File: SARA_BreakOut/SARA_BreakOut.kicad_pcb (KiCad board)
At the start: 2 copper layers, 82 parts, among them J1 USB_B, J12 Batt_conn, J13 3v8 tp, J14 1v8 tp, J15 Mechanical_slot, J16 1,2:Vusb_bat/3,4:Vxplain, J17 priority1_1,2:on/3,4:off, J18 priority2_1,2:on/3,4:off, J2 Conn_02x10_Odd_Even, J3 cur_tp, J4 txd, J5 rxd, J6 pwr_on, J7 reset_n, J8 EXT_BATT, J9 conn_to_board, SW1 SW_Push, SW2 SW_Push, U1 LSF0108, U2 LSF0108, U3 AP7361C-SOT89-5, U4 SARA-R410M-02B, U5 TLV62568A, U6 SWISSCOM_SIM

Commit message: first finish of pcb
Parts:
- removed D10: network, LEDs:LED_1206_HandSoldering
- removed D11: mod_status, LEDs:LED_1206_HandSoldering
- removed D12: sim, LEDs:LED_1206_HandSoldering
- removed D6: sara_tx, LEDs:LED_1206_HandSoldering
- removed D7: sara_rx, LEDs:LED_1206_HandSoldering
- removed D8: pwr_on, LEDs:LED_1206_HandSoldering
- removed D9: v_int, LEDs:LED_1206_HandSoldering
- removed J17: priority1_1,2:on/3,4:off, Pin_Headers:Pin_Header_Angled_2x02_Pitch2.54mm
- removed J18: priority2_1,2:on/3,4:off, Pin_Headers:Pin_Header_Angled_2x02_Pitch2.54mm
- removed R10, R11, R12, R13, R14, R15, R9: 2k, Resistors_SMD:R_1206_HandSoldering
- BT1, C24, C3, C4, C5, L1, R4, R5, R6, R7, R8, U3, U5: moved to B.Cu
- J12: footprint Pin_Headers:Pin_Header_Angled_1x02_Pitch2.54mm -> Pin_Headers:Pin_Header_Straight_1x02_Pitch2.54mm
- J16: footprint Pin_Headers:Pin_Header_Angled_2x02_Pitch2.54mm -> Pin_Headers:Pin_Header_Straight_2x02_Pitch2.54mm
- moved C14 87.6 mm to (194.1, 179.8), turned to 90 degrees
- moved C25 85.3 mm to (189.5, 179.8), turned to 90 degrees
- moved C20 83.0 mm to (184.4, 179.8), turned to 90 degrees
- moved C21 79.6 mm to (175.2, 180.0), turned to 90 degrees
- moved C18 78.0 mm to (170.7, 179.8), turned to 90 degrees
- moved C16 76.9 mm to (166.1, 179.8), turned to 90 degrees
- moved C19 76.0 mm to (161.5, 179.8), turned to 90 degrees
- moved C11 75.3 mm to (157.0, 179.8), turned to 90 degrees
- moved C22 75.3 mm to (140.2, 179.8), turned to 90 degrees
- moved C8 74.9 mm to (144.3, 179.8), turned to 90 degrees
- moved C23 74.9 mm to (152.4, 179.8), turned to 90 degrees
- moved C26 74.8 mm to (148.3, 179.8), turned to 90 degrees
- moved J2 69.6 mm to (85.7, 74.9)
- moved C27 64.5 mm to (85.9, 120.4)
- moved J16 60.7 mm to (96.6, 73.4)
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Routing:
- net /1v8: track 0.00 -> 81.0 mm, vias 0 -> 2
- net /5v: track 0.00 -> 74.0 mm, vias 0 -> 1
- net /pwr_on: track 0.00 -> 73.2 mm, vias 0 -> 2
- net /reset_n: track 0.00 -> 72.8 mm, vias 0 -> 1
- net /sim_io: track 0.00 -> 70.5 mm, vias 0 -> 2
- net /3v8: track 0.00 -> 68.2 mm, vias 0 -> 7
- net /v_int: track 0.00 -> 57.9 mm
- net /dsr: track 0.00 -> 55.3 mm
- net /vsim: track 0.00 -> 54.9 mm, vias 0 -> 2
- net /ri: track 0.00 -> 54.2 mm
- net /dcd: track 0.00 -> 52.8 mm
- net /sim_clk: track 0.00 -> 51.6 mm, vias 0 -> 2
- net /dtr: track 0.00 -> 51.5 mm
- net /txd: track 0.00 -> 50.4 mm
- net /rts: track 0.00 -> 50.2 mm
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- added copper zone on power_sig, net /3v8
- added copper zone on B.Cu, net GND
- added copper zone on F.Cu, net GND
- added copper zone on GROUND_PLANE, net GND
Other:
- copper layers 2 -> 4

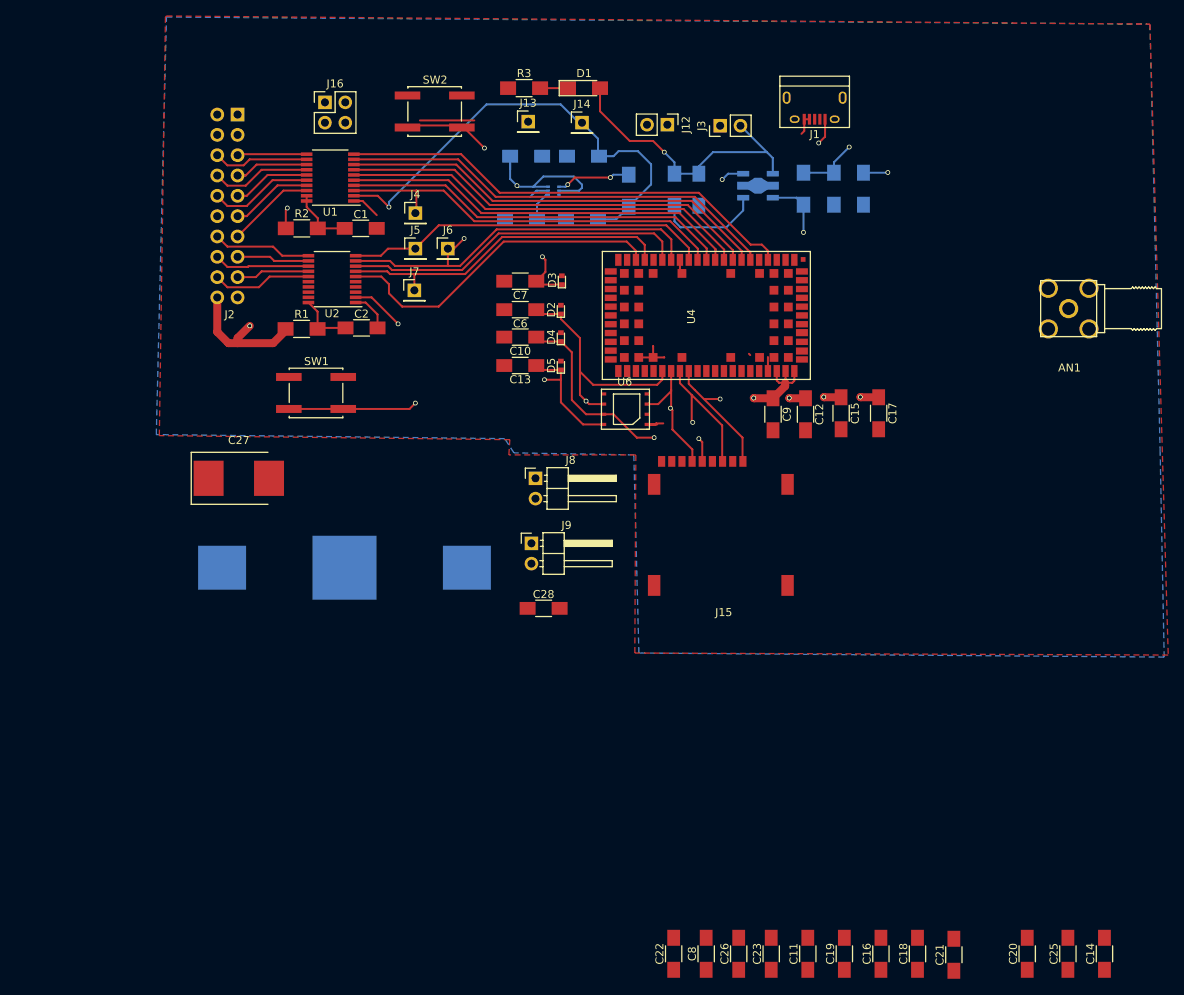
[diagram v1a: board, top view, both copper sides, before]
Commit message: pcb trimmed and shrinked
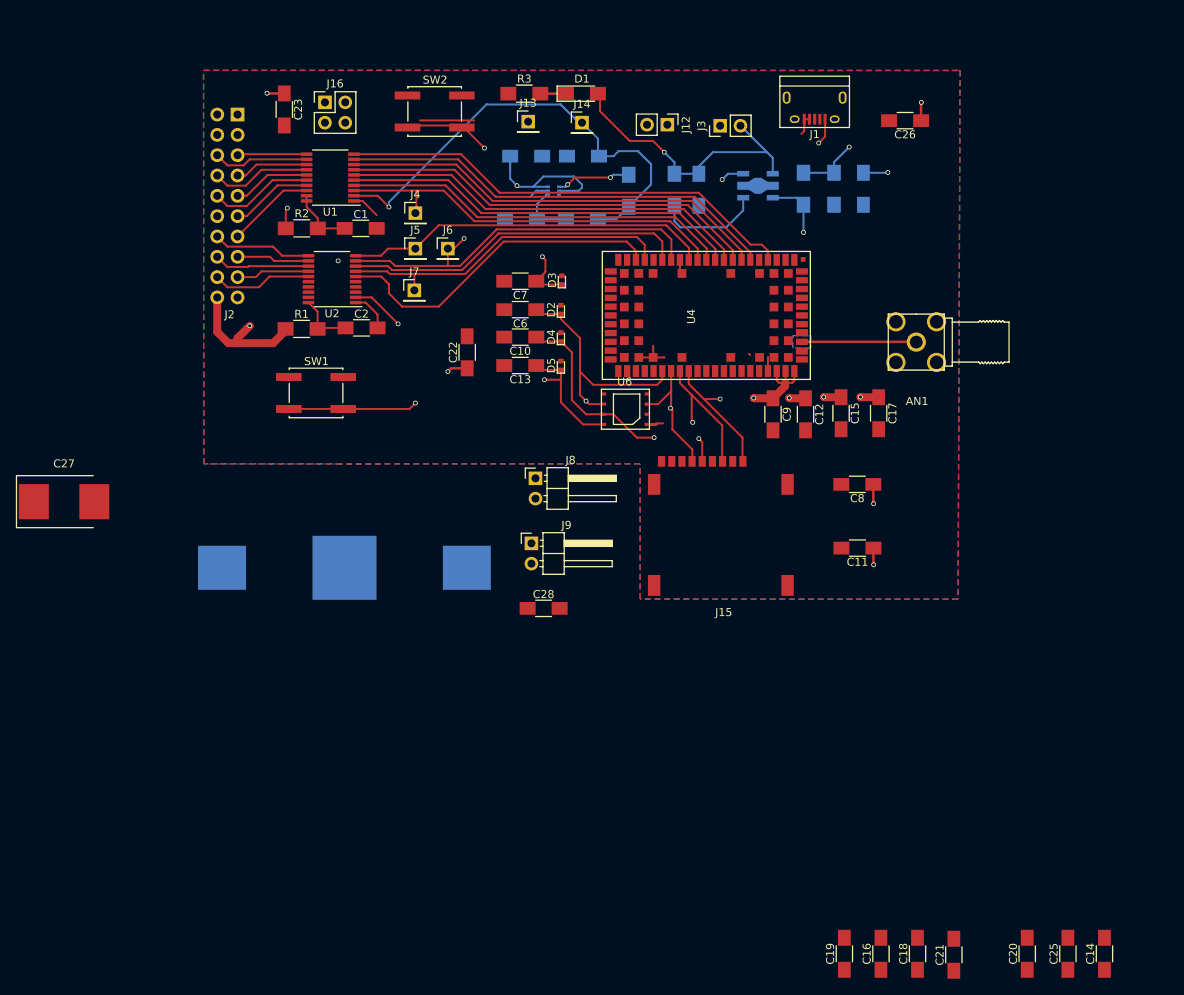
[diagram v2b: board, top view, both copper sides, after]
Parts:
- moved C23 121.8 mm to (91.5, 74.3), turned to 270 degrees
- moved C26 106.2 mm to (169.1, 75.7), turned to 180 degrees
- moved C22 79.5 mm to (114.4, 104.6)
- moved C8 61.6 mm to (163.2, 121.2), turned to 180 degrees
- moved C11 51.1 mm to (163.2, 129.1), turned to 180 degrees
- moved C27 22.0 mm to (64.0, 123.3)
- moved AN1 19.5 mm to (170.5, 103.4)
- moved D1 0.74 mm to (128.7, 72.3)
- moved R3 0.69 mm to (121.5, 72.3)
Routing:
- net Net-(AN1-Pad1): track 0.00 -> 14.4 mm
- net /3v8: track 68.2 -> 79.8 mm, vias 7 -> 12
- net (no net): vias 0 -> 1
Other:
- net class antenna added: clearance 0.25, trace_width 0.326, via_dia 0.6, via_drill 0.4

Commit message: final version 1
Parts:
- removed C14, C16, C18, C19: 10nF, Capacitors_SMD:C_1206_HandSoldering
- removed C20, C21, C25: 0.1uF, Capacitors_SMD:C_1206_HandSoldering
- added REF**: via_stitch, via_stitch:via_stitch, F.Cu at (97.9, 84.9)
- added REF**: via_stitch, via_stitch:via_stitch, F.Cu at (159.7, 104.6)
- added REF**: via_stitch, via_stitch:via_stitch, F.Cu at (171.9, 89.6)
- added REF**: via_stitch, via_stitch:via_stitch, F.Cu at (168.9, 91.1)
- added REF**: via_stitch, via_stitch:via_stitch, F.Cu at (165.9, 89.6)
- added REF**: via_stitch, via_stitch:via_stitch, F.Cu at (174.1, 115.7)
- added REF**: via_stitch, via_stitch:via_stitch, F.Cu at (174.1, 112.7)
- added REF**: via_stitch, via_stitch:via_stitch, F.Cu at (172.1, 114.2)
- added REF**: via_stitch, via_stitch:via_stitch, F.Cu at (169.1, 112.7)
- added REF**: via_stitch, via_stitch:via_stitch, F.Cu at (174.1, 109.7)
- added REF**: via_stitch, via_stitch:via_stitch, F.Cu at (172.1, 111.2)
- added REF**: via_stitch, via_stitch:via_stitch, F.Cu at (174.2, 132.3)
- added REF**: via_stitch, via_stitch:via_stitch, F.Cu at (173.1, 92.5)
- added REF**: via_stitch, via_stitch:via_stitch, F.Cu at (171.2, 133.8)
- added REF**: via_stitch, via_stitch:via_stitch, F.Cu at (174.2, 129.3)
- added REF**: via_stitch, via_stitch:via_stitch, F.Cu at (171.2, 130.8)
- added REF**: via_stitch, via_stitch:via_stitch, F.Cu at (168.2, 129.3)
- added REF**: via_stitch, via_stitch:via_stitch, F.Cu at (174.2, 126.3)
- added REF**: via_stitch, via_stitch:via_stitch, F.Cu at (171.2, 127.8)
- added REF**: via_stitch, via_stitch:via_stitch, F.Cu at (168.2, 126.3)
- added REF**: via_stitch, via_stitch:via_stitch, F.Cu at (174.2, 123.3)
- added REF**: via_stitch, via_stitch:via_stitch, F.Cu at (168.2, 123.3)
- added REF**: via_stitch, via_stitch:via_stitch, F.Cu at (174.2, 120.3)
- added REF**: via_stitch, via_stitch:via_stitch, F.Cu at (170.1, 79.7)
- added REF**: via_stitch, via_stitch:via_stitch, F.Cu at (171.2, 121.8)
- added REF**: via_stitch, via_stitch:via_stitch, F.Cu at (168.2, 120.3)
- added REF**: via_stitch, via_stitch:via_stitch, F.Cu at (171.2, 118.8)
- added REF**: via_stitch, via_stitch:via_stitch, F.Cu at (168.0, 101.6)
- added REF**: via_stitch, via_stitch:via_stitch, F.Cu at (163.7, 107.8)
- added REF**: via_stitch, via_stitch:via_stitch, F.Cu at (157.8, 107.4)
- added REF**: via_stitch, via_stitch:via_stitch, F.Cu at (160.1, 107.8)
- added REF**: via_stitch, via_stitch:via_stitch, F.Cu at (163.7, 106.0)
- added REF**: via_stitch, via_stitch:via_stitch, F.Cu at (161.9, 106.9)
- added REF**: via_stitch, via_stitch:via_stitch, F.Cu at (165.6, 104.5)
- added REF**: via_stitch, via_stitch:via_stitch, F.Cu at (173.7, 80.1)
- added REF**: via_stitch, via_stitch:via_stitch, F.Cu at (164.6, 104.5)
- added REF**: via_stitch, via_stitch:via_stitch, F.Cu at (168.2, 117.3)
- added REF**: via_stitch, via_stitch:via_stitch, F.Cu at (169.1, 109.7)
- added REF**: via_stitch, via_stitch:via_stitch, F.Cu at (163.6, 104.6)
- added REF**: via_stitch, via_stitch:via_stitch, F.Cu at (162.6, 104.5)
- added REF**: via_stitch, via_stitch:via_stitch, F.Cu at (161.7, 104.5)
- added REF**: via_stitch, via_stitch:via_stitch, F.Cu at (160.7, 104.5)
- added REF**: via_stitch, via_stitch:via_stitch, F.Cu at (158.7, 104.6)
- added REF**: via_stitch, via_stitch:via_stitch, F.Cu at (158.3, 102.1)
- added REF**: via_stitch, via_stitch:via_stitch, F.Cu at (160.3, 102.1)
- added REF**: via_stitch, via_stitch:via_stitch, F.Cu at (170.8, 83.0)
- added REF**: via_stitch, via_stitch:via_stitch, F.Cu at (161.3, 102.2)
- added REF**: via_stitch, via_stitch:via_stitch, F.Cu at (162.3, 102.2)
- added REF**: via_stitch, via_stitch:via_stitch, F.Cu at (163.3, 102.2)
- added REF**: via_stitch, via_stitch:via_stitch, F.Cu at (164.2, 102.2)
- added REF**: via_stitch, via_stitch:via_stitch, F.Cu at (165.2, 102.2)
- added REF**: via_stitch, via_stitch:via_stitch, F.Cu at (166.2, 102.2)
- added REF**: via_stitch, via_stitch:via_stitch, F.Cu at (160.1, 106.0)
- added REF**: via_stitch, via_stitch:via_stitch, F.Cu at (138.2, 97.6)
- added REF**: via_stitch, via_stitch:via_stitch, F.Cu at (173.1, 84.8)
- added REF**: via_stitch, via_stitch:via_stitch, F.Cu at (168.9, 86.8)
- added REF**: via_stitch, via_stitch:via_stitch, F.Cu at (160.8, 99.3)
- added REF**: via_stitch, via_stitch:via_stitch, F.Cu at (102.7, 116.8)
- added REF**: via_stitch, via_stitch:via_stitch, F.Cu at (98.0, 116.0)
- added REF**: via_stitch, via_stitch:via_stitch, F.Cu at (96.6, 83.4)
- added REF**: via_stitch, via_stitch:via_stitch, F.Cu at (90.8, 116.7)
- added REF**: via_stitch, via_stitch:via_stitch, F.Cu at (84.3, 115.2)
- added REF**: via_stitch, via_stitch:via_stitch, F.Cu at (87.9, 113.0)
- added REF**: via_stitch, via_stitch:via_stitch, F.Cu at (83.1, 110.9)
- added REF**: via_stitch, via_stitch:via_stitch, F.Cu at (86.0, 109.7)
- added REF**: via_stitch, via_stitch:via_stitch, F.Cu at (87.9, 107.0)
- added REF**: via_stitch, via_stitch:via_stitch, F.Cu at (84.1, 106.9)
- added REF**: via_stitch, via_stitch:via_stitch, F.Cu at (107.0, 115.4)
- added REF**: via_stitch, via_stitch:via_stitch, F.Cu at (102.9, 114.2)
- added REF**: via_stitch, via_stitch:via_stitch, F.Cu at (103.1, 108.9)
- added REF**: via_stitch, via_stitch:via_stitch, F.Cu at (98.1, 82.0)
- added REF**: via_stitch, via_stitch:via_stitch, F.Cu at (106.2, 107.5)
- added REF**: via_stitch, via_stitch:via_stitch, F.Cu at (110.0, 102.6)
- added REF**: via_stitch, via_stitch:via_stitch, F.Cu at (103.6, 104.8)
- added REF**: via_stitch, via_stitch:via_stitch, F.Cu at (134.9, 111.8)
- added REF**: via_stitch, via_stitch:via_stitch, F.Cu at (133.8, 110.4)
- added REF**: via_stitch, via_stitch:via_stitch, F.Cu at (123.7, 116.1)
- added REF**: via_stitch, via_stitch:via_stitch, F.Cu at (117.3, 116.1)
- added REF**: via_stitch, via_stitch:via_stitch, F.Cu at (110.9, 116.1)
- added REF**: via_stitch, via_stitch:via_stitch, F.Cu at (123.7, 112.9)
- added REF**: via_stitch, via_stitch:via_stitch, F.Cu at (120.5, 114.5)
- added REF**: via_stitch, via_stitch:via_stitch, F.Cu at (96.8, 80.3)
- added REF**: via_stitch, via_stitch:via_stitch, F.Cu at (117.3, 112.9)
- added REF**: via_stitch, via_stitch:via_stitch, F.Cu at (114.1, 114.5)
- added REF**: via_stitch, via_stitch:via_stitch, F.Cu at (110.9, 112.9)
- added REF**: via_stitch, via_stitch:via_stitch, F.Cu at (120.5, 111.3)
- added REF**: via_stitch, via_stitch:via_stitch, F.Cu at (114.1, 111.3)
- added REF**: via_stitch, via_stitch:via_stitch, F.Cu at (110.9, 109.7)
- added REF**: via_stitch, via_stitch:via_stitch, F.Cu at (150.3, 100.6)
- added REF**: via_stitch, via_stitch:via_stitch, F.Cu at (147.5, 102.2)
- added REF**: via_stitch, via_stitch:via_stitch, F.Cu at (144.4, 100.7)
- added REF**: via_stitch, via_stitch:via_stitch, F.Cu at (141.3, 102.2)
- added REF**: via_stitch, via_stitch:via_stitch, F.Cu at (98.0, 97.6)
- added REF**: via_stitch, via_stitch:via_stitch, F.Cu at (138.2, 100.7)
- added REF**: via_stitch, via_stitch:via_stitch, F.Cu at (150.3, 97.5)
- added REF**: via_stitch, via_stitch:via_stitch, F.Cu at (147.5, 99.1)
- added REF**: via_stitch, via_stitch:via_stitch, F.Cu at (144.4, 97.6)
- added REF**: via_stitch, via_stitch:via_stitch, F.Cu at (141.3, 99.1)
- added REF**: via_stitch, via_stitch:via_stitch, F.Cu at (152.3, 132.8)
- added REF**: via_stitch, via_stitch:via_stitch, F.Cu at (149.3, 134.3)
- added REF**: via_stitch, via_stitch:via_stitch, F.Cu at (146.3, 132.8)
- added REF**: via_stitch, via_stitch:via_stitch, F.Cu at (143.3, 134.3)
- added REF**: via_stitch, via_stitch:via_stitch, F.Cu at (140.3, 132.8)
- added REF**: via_stitch, via_stitch:via_stitch, F.Cu at (96.7, 95.9)
- added REF**: via_stitch, via_stitch:via_stitch, F.Cu at (152.3, 129.8)
- added REF**: via_stitch, via_stitch:via_stitch, F.Cu at (149.3, 131.3)
- added REF**: via_stitch, via_stitch:via_stitch, F.Cu at (146.3, 129.8)
- added REF**: via_stitch, via_stitch:via_stitch, F.Cu at (140.3, 129.8)
- added REF**: via_stitch, via_stitch:via_stitch, F.Cu at (152.3, 126.8)
- added REF**: via_stitch, via_stitch:via_stitch, F.Cu at (146.3, 126.8)
- added REF**: via_stitch, via_stitch:via_stitch, F.Cu at (143.3, 128.3)
- added REF**: via_stitch, via_stitch:via_stitch, F.Cu at (140.3, 126.8)
- added REF**: via_stitch, via_stitch:via_stitch, F.Cu at (152.3, 123.8)
- added REF**: via_stitch, via_stitch:via_stitch, F.Cu at (149.3, 125.3)
- added REF**: via_stitch, via_stitch:via_stitch, F.Cu at (98.3, 94.3)
- added REF**: via_stitch, via_stitch:via_stitch, F.Cu at (146.3, 123.8)
- added REF**: via_stitch, via_stitch:via_stitch, F.Cu at (143.3, 125.3)
- added REF**: via_stitch, via_stitch:via_stitch, F.Cu at (140.3, 123.8)
- added REF**: via_stitch, via_stitch:via_stitch, F.Cu at (152.3, 120.8)
- added REF**: via_stitch, via_stitch:via_stitch, F.Cu at (146.3, 120.8)
- added REF**: via_stitch, via_stitch:via_stitch, F.Cu at (140.3, 120.8)
- added REF**: via_stitch, via_stitch:via_stitch, F.Cu at (151.6, 118.5)
- added REF**: via_stitch, via_stitch:via_stitch, F.Cu at (154.8, 117.6)
- added REF**: via_stitch, via_stitch:via_stitch, F.Cu at (167.3, 134.4)
- added REF**: via_stitch, via_stitch:via_stitch, F.Cu at (164.2, 133.4)
- added REF**: via_stitch, via_stitch:via_stitch, F.Cu at (96.9, 93.0)
- added REF**: via_stitch, via_stitch:via_stitch, F.Cu at (165.1, 125.9)
- added REF**: via_stitch, via_stitch:via_stitch, F.Cu at (161.1, 125.7)
- added REF**: via_stitch, via_stitch:via_stitch, F.Cu at (165.1, 117.5)
- added REF**: via_stitch, via_stitch:via_stitch, F.Cu at (161.2, 117.5)
- added REF**: via_stitch, via_stitch:via_stitch, F.Cu at (160.6, 133.6)
- added REF**: via_stitch, via_stitch:via_stitch, F.Cu at (157.9, 132.6)
- added REF**: via_stitch, via_stitch:via_stitch, F.Cu at (157.9, 129.6)
- added REF**: via_stitch, via_stitch:via_stitch, F.Cu at (157.9, 126.6)
- added REF**: via_stitch, via_stitch:via_stitch, F.Cu at (157.9, 123.6)
- added REF**: via_stitch, via_stitch:via_stitch, F.Cu at (157.9, 120.6)
- added REF**: via_stitch, via_stitch:via_stitch, F.Cu at (159.3, 102.1)
- added REF**: via_stitch, via_stitch:via_stitch, F.Cu at (157.9, 117.6)
- added REF**: via_stitch, via_stitch:via_stitch, F.Cu at (171.9, 95.6)
- added REF**: via_stitch, via_stitch:via_stitch, F.Cu at (168.9, 97.1)
- added REF**: via_stitch, via_stitch:via_stitch, F.Cu at (165.9, 95.6)
- added REF**: via_stitch, via_stitch:via_stitch, F.Cu at (162.9, 97.1)
- added REF**: via_stitch, via_stitch:via_stitch, F.Cu at (159.9, 95.6)
- added REF**: via_stitch, via_stitch:via_stitch, F.Cu at (168.9, 94.1)
- added REF**: via_stitch, via_stitch:via_stitch, F.Cu at (165.9, 92.6)
- added REF**: via_stitch, via_stitch:via_stitch, F.Cu at (162.9, 94.1)
- added REF**: via_stitch, via_stitch:via_stitch, F.Cu at (159.9, 92.6)
- J8, J9: footprint Pin_Headers:Pin_Header_Angled_1x02_Pitch2.54mm -> Pin_Headers:Pin_Header_Straight_1x02_Pitch2.54mm
- moved J9 38.8 mm to (83.7, 128.0), turned to 180 degrees
- moved C27 37.5 mm to (101.3, 127.9), turned to 270 degrees
- moved C28 13.2 mm to (114.0, 128.0), turned to 90 degrees
- moved J8 11.1 mm to (131.3, 127.7), turned to 180 degrees
- moved BT1 10.7 mm to (108.6, 126.6)
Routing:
- net /Batt_and_LEDs/BATT_GND: track 0.00 -> 27.0 mm, vias 0 -> 2
- net /Batt_and_LEDs/BATT_V: track 0.00 -> 18.1 mm
- net /sim_clk: track 51.6 -> 52.6 mm
- net Net-(C2-Pad1): track 7.32 -> 7.97 mm
- net (no net): vias 1 -> 4
- added copper zone on B.Cu, net /Batt_and_LEDs/BATT_GND
- added copper zone on F.Cu, net /Batt_and_LEDs/BATT_V
